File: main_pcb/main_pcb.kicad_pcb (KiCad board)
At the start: 2 copper layers, 65 x 56 mm, 7 parts, among them J1 Conn_01x17, J2 Conn_01x17, P1 Conn_02x20_Odd_Even

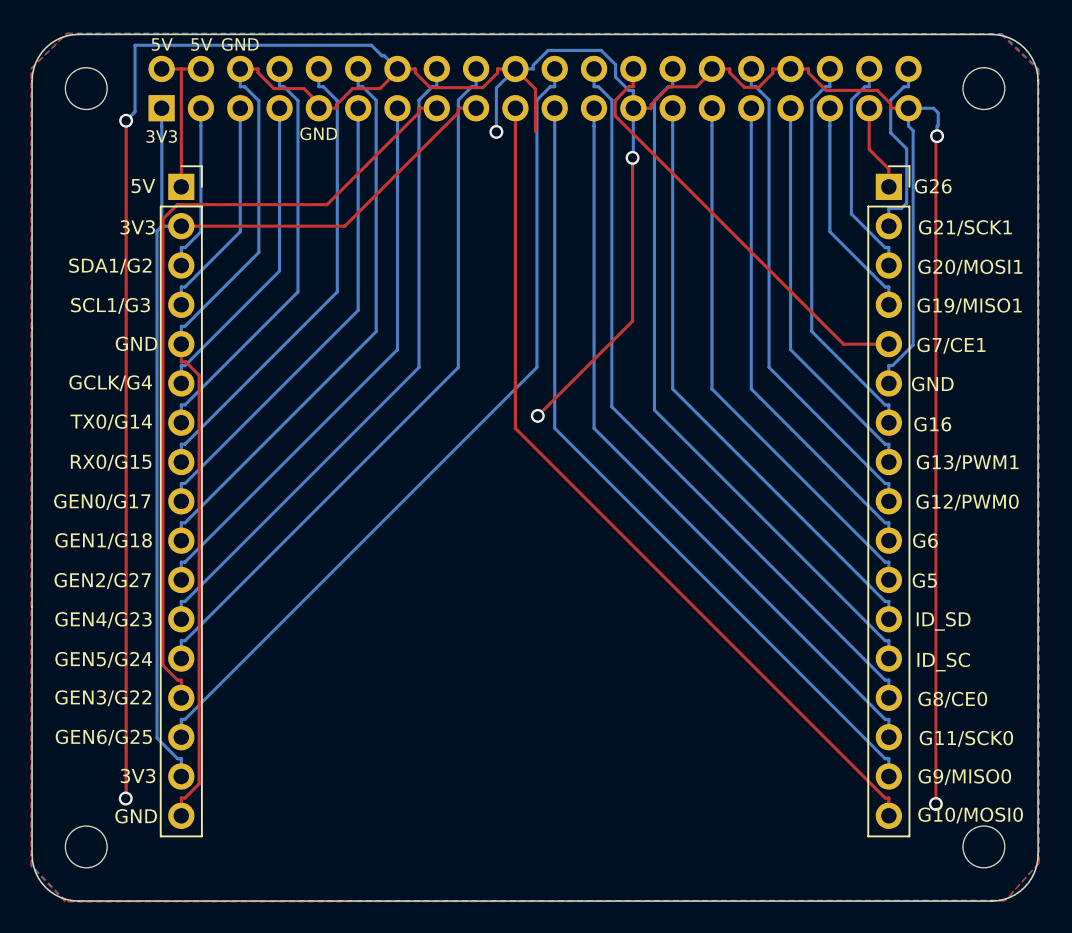
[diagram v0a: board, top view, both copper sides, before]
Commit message: Correct hole position of main_pcb
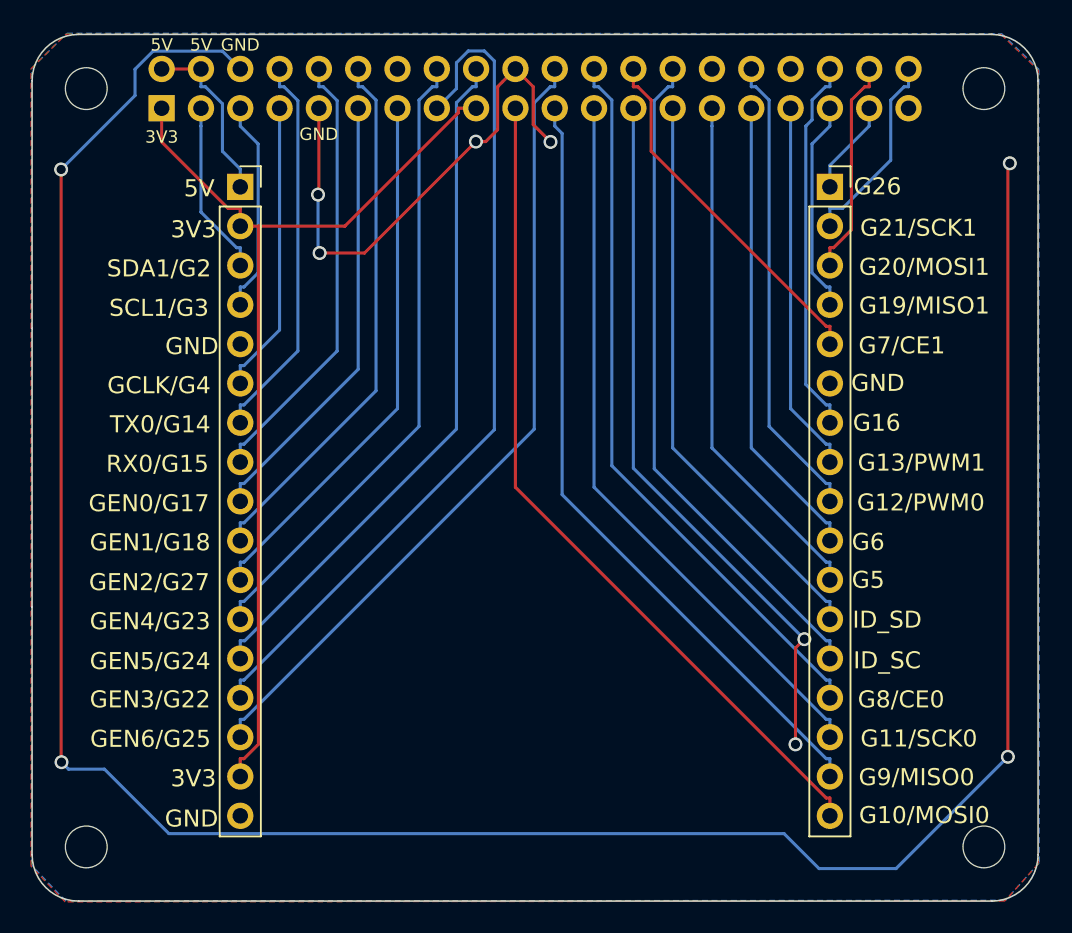
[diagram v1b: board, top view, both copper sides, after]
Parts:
- moved J1 3.81 mm to (213.4, 103.8)
- moved J2 3.81 mm to (251.6, 103.8)
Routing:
- net GND: track 270.6 -> 240.1 mm, vias 7 -> 10
- net /GPIO7(SPI1_CE_N): track 27.5 -> 23.3 mm
- net +3V3: track 67.7 -> 64.9 mm
- net /GPIO22(GEN3): track 52.4 -> 54.6 mm
- net /GPIO15(RXD0): track 30.4 -> 28.8 mm
- net /GPIO18(GEN1)(PWM0): track 36.5 -> 34.9 mm
- net /GPIO14(TXD0): track 26.8 -> 25.2 mm
- net /GPIO25(GEN6): track 53.5 -> 51.9 mm
- net /GPIO8(SPI0_CE_N): track 48.8 -> 47.3 mm
- net /GPIO23(GEN4): track 42.7 -> 41.1 mm
- net /GPIO17(GEN0): track 30.3 -> 28.7 mm
- net /GPIO11(SPI0_SCK): track 48.7 -> 47.1 mm
- net /GPIO10(SPI0_MOSI): track 55.9 -> 54.3 mm
- net /GPIO6: track 31.8 -> 30.2 mm
- net /GPIO4(GCLK): track 20.5 -> 19.0 mm
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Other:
- board text added: "Rev2020.01"
- board text removed: "Rev2019.12"

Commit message: Apply header footprints to main pcb
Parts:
- P1: footprint Connector_PinSocket_2.54mm:PinSocket_2x20_P2.54mm_Vertical -> Connector_PinHeader_2.54mm:PinHeader_2x20_P2.54mm_Vertical; moved to F.Cu
- turned P1 to 90 degrees
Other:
- board text added: "Rev2020.05"
- board text removed: "Rev2020.01"
